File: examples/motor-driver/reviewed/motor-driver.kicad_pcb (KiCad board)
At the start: 2 copper layers, 100 x 50 mm, 12 parts, among them J1 VM 2.7-10.8V, J2 MOTOR A, J3 MOTOR B, J4 LOGIC, U1 DRV8833PW

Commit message: Regenerate the five with stitched pours, silk that speaks, and wires that never double back
All ten variants rebuilt by the fixed generator: reviewed boards carry
ground on both faces with the stitching ring (buck 35 vias, fpga 116),
thru_hole_only front pours, the board id and connector pin names in
silk, and the buck's explicit ground return; the sheets hook power up
through upright symbols and source-anchored flags with no overlapping
wires and no junction-less tees left. Every reviewed variant passes its
own gate with zero errors; every as-generated variant still fails, now
also for the rules this round added.

Co-Authored-By: Claude Fable 5 <noreply@anthropic.com>
Claude-Session: https://claude.ai/code/session_01DUj7Ltu92tWg159mCSacwY
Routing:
- net GND: vias 10 -> 37
- added copper zone on F.Cu, net GND
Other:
- board text added: "AIN1"
- board text added: "AIN2"
- board text added: "AOUT1"
- board text added: "AOUT2"
- board text added: "BIN1"
- board text added: "BIN2"
- board text added: "BOUT1"
- board text added: "BOUT2"
- board text added: "GND"
- board text added: "VM"
- board text added: "VM OK"
- board text added: "motor-driver rev A"
- board text added: "nFAULT"
- board text added: "nSLEEP"
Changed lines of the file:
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@@
 	(via (at 160.75 93.0) (size 0.8) (drill 0.4) (layers "F.Cu" "B.Cu") (net 6))
 	(via (at 163.0 95.25) (size 0.8) (drill 0.4) (layers "F.Cu" "B.Cu") (net 6))
+	(via (at 104.5 64.5) (size 0.8) (drill 0.4) (layers "F.Cu" "B.Cu") (net 1))
+	(via (at 104.5 105.5) (size 0.8) (drill 0.4) (layers "F.Cu" "B.Cu") (net 1))
+	(via (at 114.5 64.5) (size 0.8) (drill 0.4) (layers "F.Cu" "B.Cu") (net 1))
+	(via (at 114.5 105.5) (size 0.8) (drill 0.4) (layers "F.Cu" "B.Cu") (net 1))
+	(via (at 124.5 64.5) (size 0.8) (drill 0.4) (layers "F.Cu" "B.Cu") (net 1))
+	(via (at 124.5 105.5) (size 0.8) (drill 0.4) (layers "F.Cu" "B.Cu") (net 1))
+	(via (at 134.5 64.5) (size 0.8) (drill 0.4) (layers "F.Cu" "B.Cu") (net 1))
+	(via (at 134.5 105.5) (size 0.8) (drill 0.4) (layers "F.Cu" "B.Cu") (net 1))
+	(via (at 144.5 64.5) (size 0.8) (drill 0.4) (layers "F.Cu" "B.Cu") (net 1))
+	(via (at 144.5 105.5) (size 0.8) (drill 0.4) (layers "F.Cu" "B.Cu") (net 1))
+	(via (at 154.5 64.5) (size 0.8) (drill 0.4) (layers "F.Cu" "B.Cu") (net 1))
+	(via (at 154.5 105.5) (size 0.8) (drill 0.4) (layers "F.Cu" "B.Cu") (net 1))
+	(via (at 164.5 64.5) (size 0.8) (drill 0.4) (layers "F.Cu" "B.Cu") (net 1))
+	(via (at 164.5 105.5) (size 0.8) (drill 0.4) (layers "F.Cu" "B.Cu") (net 1))
+	(via (at 174.5 64.5) (size 0.8) (drill 0.4) (layers "F.Cu" "B.Cu") (net 1))
+	(via (at 174.5 105.5) (size 0.8) (drill 0.4) (layers "F.Cu" "B.Cu") (net 1))
+	(via (at 184.5 64.5) (size 0.8) (drill 0.4) (layers "F.Cu" "B.Cu") (net 1))
+	(via (at 184.5 105.5) (size 0.8) (drill 0.4) (layers "F.Cu" "B.Cu") (net 1))
+	(via (at 194.5 64.5) (size 0.8) (drill 0.4) (layers "F.Cu" "B.Cu") (net 1))
+	(via (at 194.5 105.5) (size 0.8) (drill 0.4) (layers "F.Cu" "B.Cu") (net 1))
+	(via (at 104.5 74.5) (size 0.8) (drill 0.4) (layers "F.Cu" "B.Cu") (net 1))
+	(via (at 195.5 74.5) (size 0.8) (drill 0.4) (layers "F.Cu" "B.Cu") (net 1))
+	(via (at 104.5 84.5) (size 0.8) (drill 0.4) (layers "F.Cu" "B.Cu") (net 1))
+	(via (at 195.5 84.5) (size 0.8) (drill 0.4) (layers "F.Cu" "B.Cu") (net 1))
+	(via (at 104.5 94.5) (size 0.8) (drill 0.4) (layers "F.Cu" "B.Cu") (net 1))
+	(via (at 195.5 94.5) (size 0.8) (drill 0.4) (layers "F.Cu" "B.Cu") (net 1))
+	(via (at 195.5 104.5) (size 0.8) (drill 0.4) (layers "F.Cu" "B.Cu") (net 1))
 	(zone
 		(net 1)
@@
 		(polygon (pts (xy 103.0 63.0) (xy 197.0 63.0) (xy 197.0 107.0) (xy 103.0 107.0)))
 	)
+	(zone
+		(net 1)
+		(net_name "GND")
+		(layer "F.Cu")
+		(hatch edge 0.5)
+		(connect_pads thru_hole_only
+			(clearance 0.4)
+		)
+		(min_thickness 0.175)
+		(filled_areas_thickness no)
+		(fill yes
+			(thermal_gap 0.5)
+			(thermal_bridge_width 0.5)
+		)
+		(polygon (pts (xy 103.0 63.0) (xy 197.0 63.0) (xy 197.0 107.0) (xy 103.0 107.0)))
+	)
+	(gr_text "motor-driver rev A" (at 150.0 107.8 0) (layer "F.SilkS") (effects (font (size 1.0 1.0) (thickness 0.15))))
+	(gr_text "VM" (at 185.3 72.0 0) (layer "F.SilkS") (effects (font (size 0.8 0.8) (thickness 0.12))))
+	(gr_text "GND" (at 185.3 77.0 0) (layer "F.SilkS") (effects (font (size 0.8 0.8) (thickness 0.12))))
+	(gr_text "VM OK" (at 180.0 68.6 0) (layer "F.SilkS") (effects (font (size 0.8 0.8) (thickness 0.12))))
+	(gr_text "AOUT2" (at 114.7 80.0 0) (layer "F.SilkS") (effects (font (size 0.8 0.8) (thickness 0.12))))
+	(gr_text "AOUT1" (at 114.7 75.0 0) (layer "F.SilkS") (effects (font (size 0.8 0.8) (thickness 0.12))))
+	(gr_text "BOUT1" (at 114.7 98.0 0) (layer "F.SilkS") (effects (font (size 0.8 0.8) (thickness 0.12))))
+	(gr_text "BOUT2" (at 114.7 93.0 0) (layer "F.SilkS") (effects (font (size 0.8 0.8) (thickness 0.12))))
+	(gr_text "GND" (at 188.63 86.0 0) (layer "F.SilkS") (effects (font (size 0.8 0.8) (thickness 0.12))))
+	(gr_text "nSLEEP" (at 188.63 88.54 0) (layer "F.SilkS") (effects (font (size 0.8 0.8) (thickness 0.12))))
+	(gr_text "AIN1" (at 188.63 91.08 0) (layer "F.SilkS") (effects (font (size 0.8 0.8) (thickness 0.12))))
+	(gr_text "AIN2" (at 188.63 93.62 0) (layer "F.SilkS") (effects (font (size 0.8 0.8) (thickness 0.12))))
+	(gr_text "BIN2" (at 188.63 96.16 0) (layer "F.SilkS") (effects (font (size 0.8 0.8) (thickness 0.12))))
+	(gr_text "BIN1" (at 188.63 98.7 0) (layer "F.SilkS") (effects (font (size 0.8 0.8) (thickness 0.12))))
+	(gr_text "nFAULT" (at 188.63 101.24 0) (layer "F.SilkS") (effects (font (size 0.8 0.8) (thickness 0.12))))
+	(gr_text "GND" (at 188.63 103.78 0) (layer "F.SilkS") (effects (font (size 0.8 0.8) (thickness 0.12))))
 )

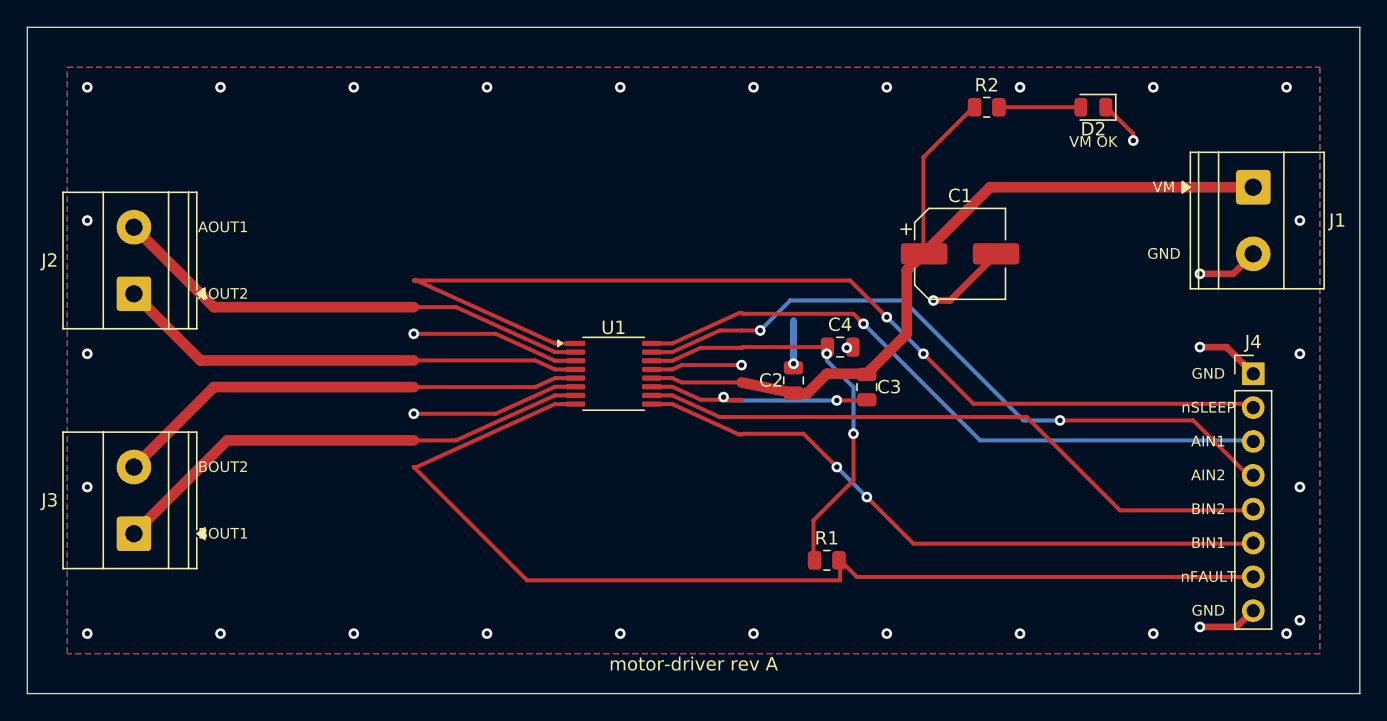
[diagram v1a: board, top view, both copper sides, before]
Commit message: Regenerate the five as round three drew them
All five reviewed projects pass their gates again: the buck all wire
with its feedback drawn home, the motor's logic named at the header,
the carrier reading as the pinout table it is - with its feed diode
finally pointing the right way - the filter compact with test points,
and the FPGA's capacitors sitting beside the units they feed. Thirty
renders redrawn, verdict tables at today's numbers.

Co-Authored-By: Claude Fable 5 <noreply@anthropic.com>
Claude-Session: https://claude.ai/code/session_01DUj7Ltu92tWg159mCSacwY
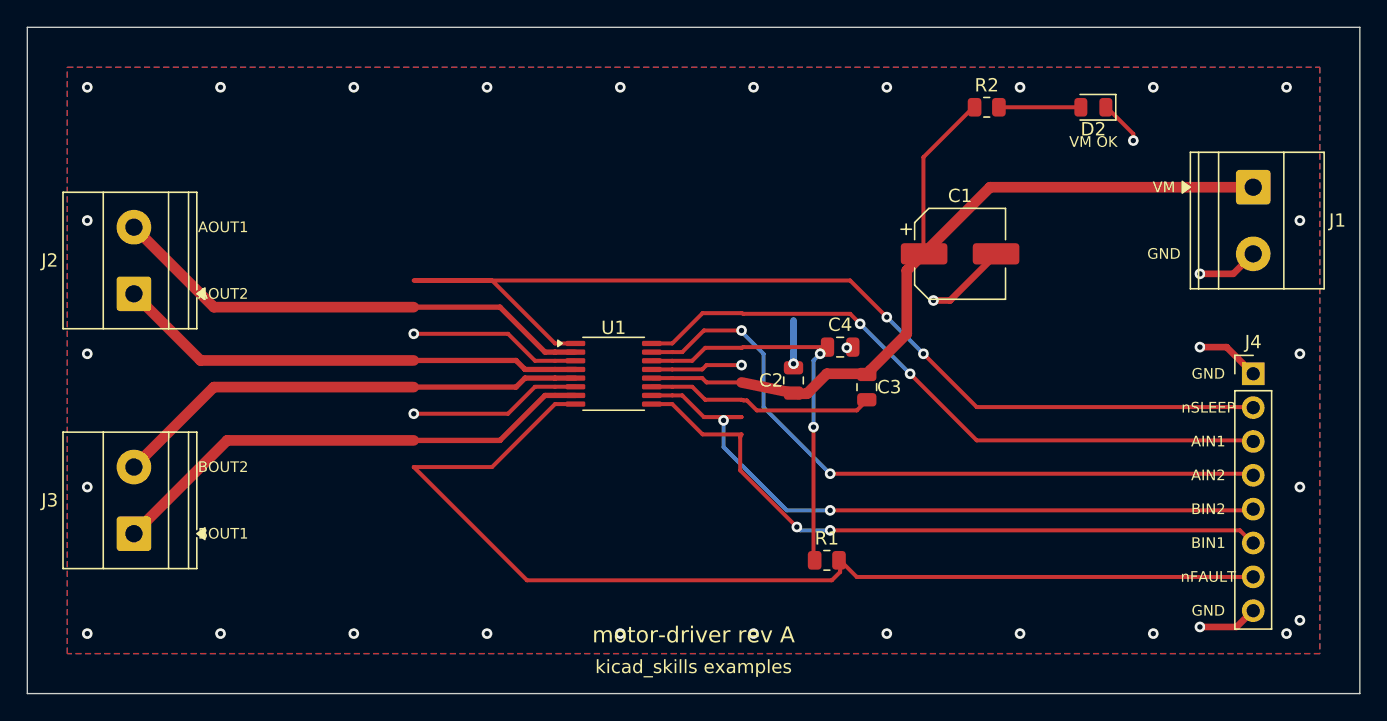
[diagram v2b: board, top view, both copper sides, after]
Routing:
- net /BIN2: track 48.4 -> 52.7 mm, vias 0 -> 2
- net /BIN1: track 49.1 -> 51.1 mm
- net /VCP: track 19.3 -> 17.2 mm, vias 2 -> 0
- net /VINT: track 31.5 -> 30.1 mm
- net /nSLEEP: track 80.1 -> 81.0 mm
- net GND: track 59.5 -> 60.3 mm
- net /AIN2: track 51.8 -> 52.7 mm
- net /BOUT1: track 36.8 -> 37.4 mm
- net /AOUT1: track 36.4 -> 37.0 mm
- net /nFAULT: track 81.8 -> 82.3 mm
- net /AIN1: track 49.6 -> 50.0 mm, vias 1 -> 2
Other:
- board text added: "kicad_skills examples"

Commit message: Regenerate the four boards round four has settled
The buck, the motor driver, the carrier and the filter as the current
generator draws them: interior ground stitching on all four, the motor
driver's bundle tight and its board twelve millimetres shorter, the
filter compact and hand-placed, the carrier's indicator in a column of
its own. All four pass their gates. The FPGA is still regenerating.

Co-Authored-By: Claude Fable 5 <noreply@anthropic.com>
Claude-Session: https://claude.ai/code/session_01DUj7Ltu92tWg159mCSacwY
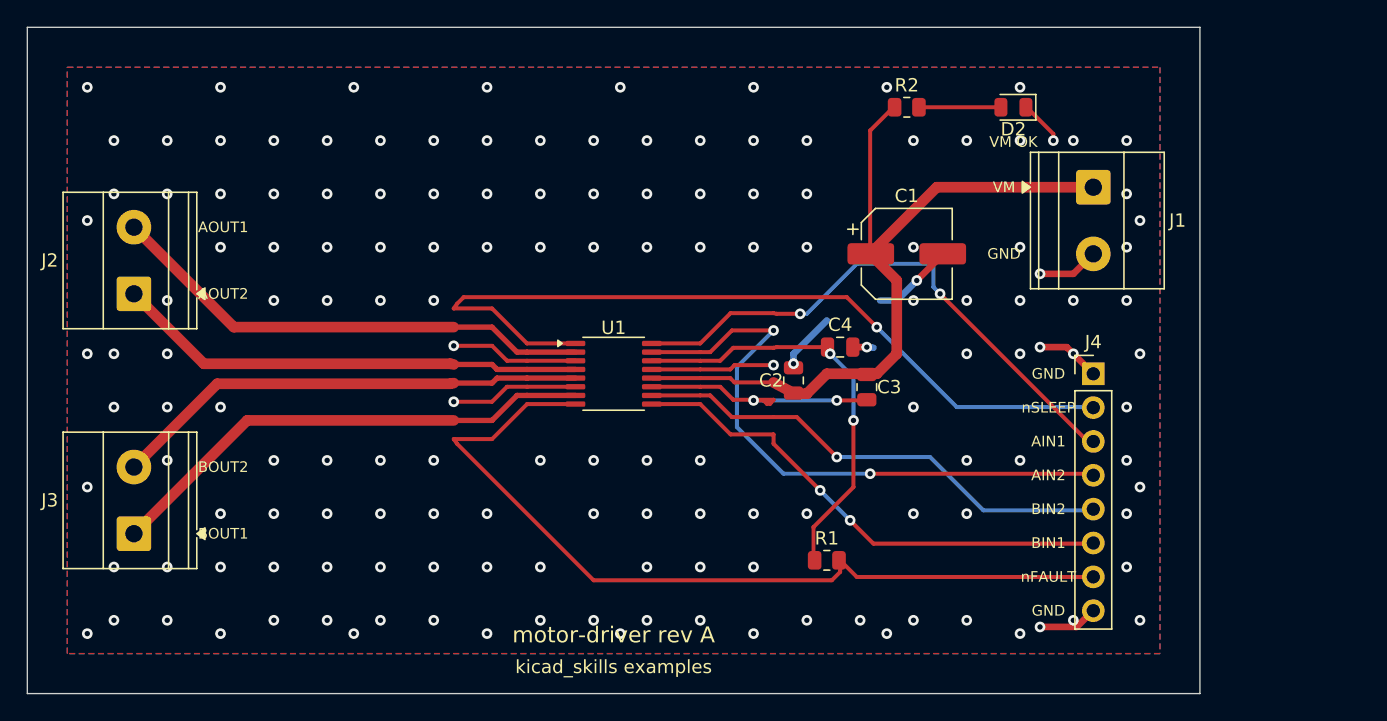
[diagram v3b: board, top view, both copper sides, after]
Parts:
- moved J1 12.0 mm to (180.0, 72.0)
- moved J4 12.0 mm to (180.0, 86.0)
- moved D2 6.00 mm to (174.0, 66.0)
- moved R2 6.00 mm to (166.0, 66.0)
- moved C1 4.00 mm to (166.0, 77.0)
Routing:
- net /nSLEEP: track 81.0 -> 62.0 mm, vias 2 -> 1
- net /nFAULT: track 82.3 -> 64.4 mm
- net /BIN2: track 52.7 -> 36.7 mm, vias 2 -> 1
- net /BIN1: track 51.1 -> 37.9 mm
- net /VM: track 67.2 -> 58.9 mm
- net /AIN1: track 50.0 -> 42.2 mm
- net /AIN2: track 52.7 -> 46.4 mm
- net /VCP: track 17.2 -> 19.8 mm, vias 0 -> 2
- net GND: track 60.3 -> 58.1 mm, vias 37 -> 156
- net /VINT: track 30.1 -> 31.7 mm
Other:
- board size 100 x 50 mm -> 88 x 50 mm

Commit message: Regenerate the four boards whose corners were off the grid
Ninety-one bends at angles nobody chose, now none. All four still pass
their gates.

Co-Authored-By: Claude Fable 5 <noreply@anthropic.com>
Claude-Session: https://claude.ai/code/session_01DUj7Ltu92tWg159mCSacwY
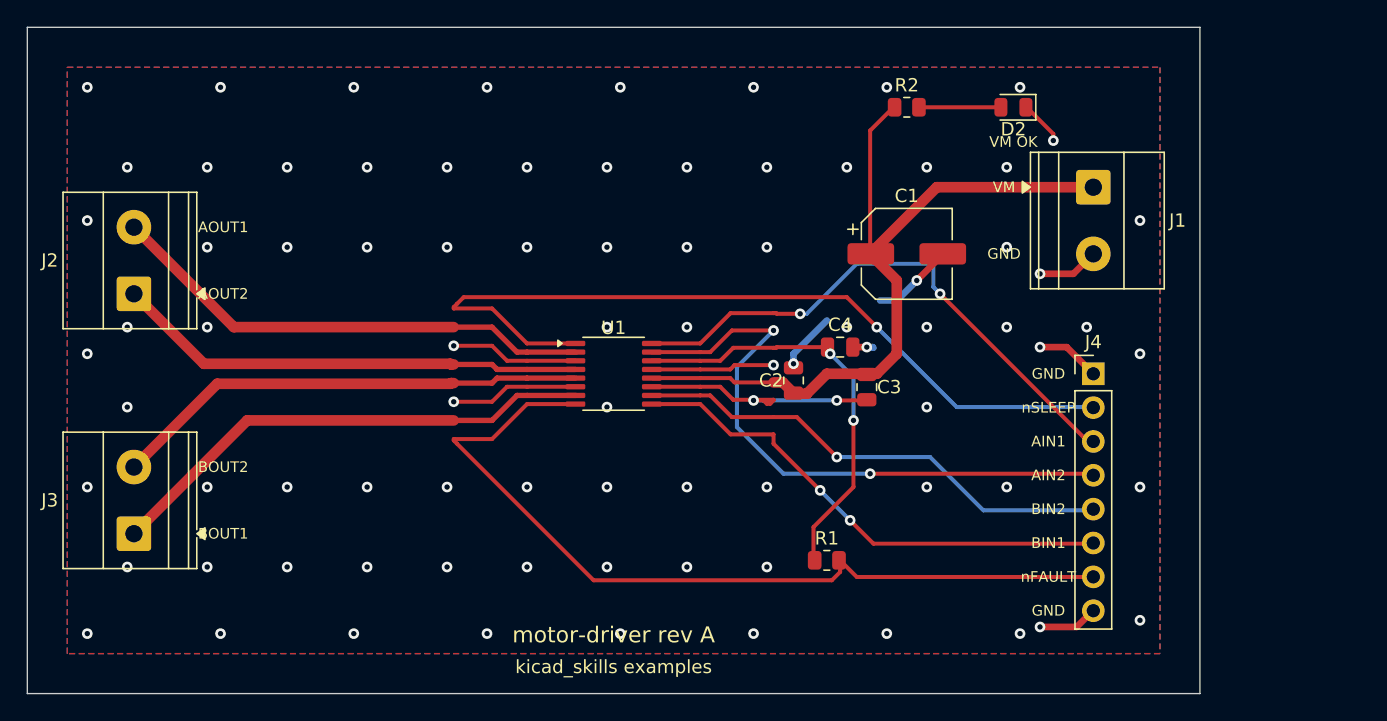
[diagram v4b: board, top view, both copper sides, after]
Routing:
- net GND: track 58.1 -> 58.2 mm, vias 156 -> 84

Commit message: Regenerate the four the text and width work changed
Designators and values off the rails they were printed on, power-named
nets at the width their rule asks for, and the buck's feedback ending
on the capacitor pad it senses at.

Co-Authored-By: Claude Fable 5 <noreply@anthropic.com>
Claude-Session: https://claude.ai/code/session_01DUj7Ltu92tWg159mCSacwY
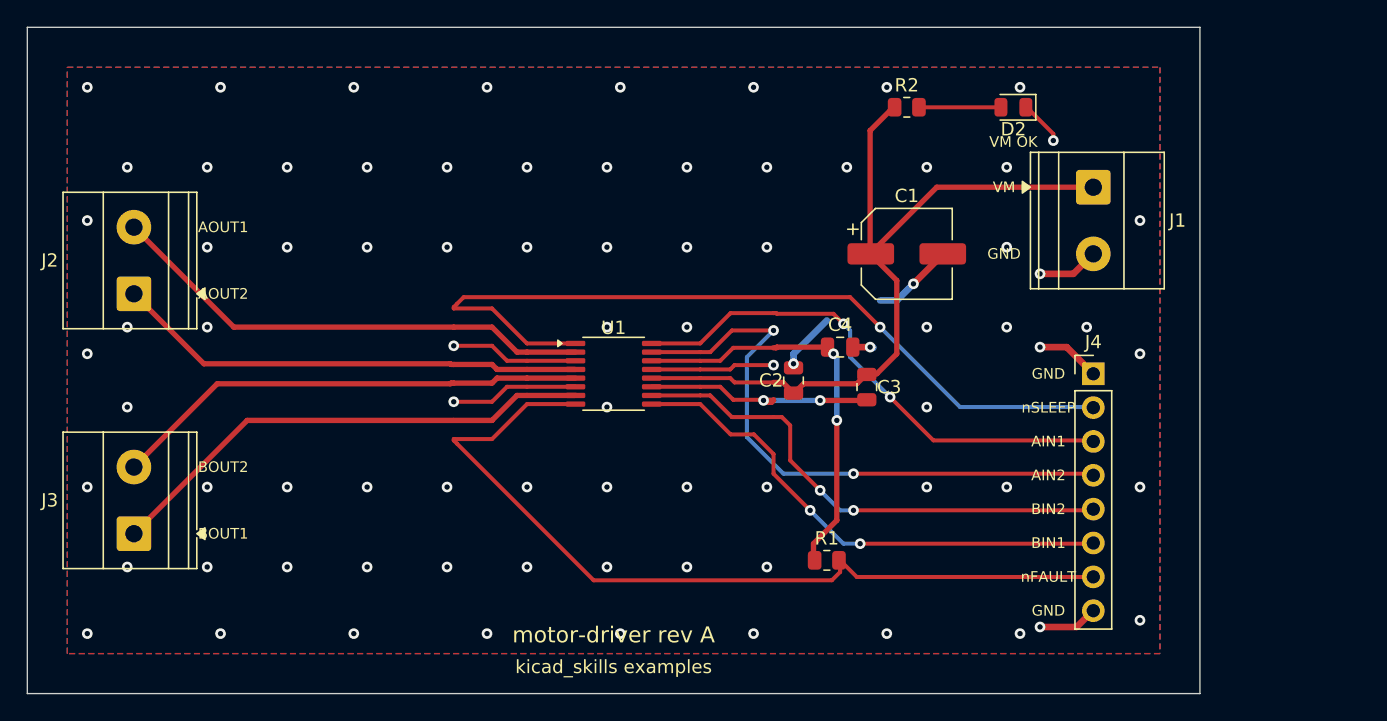
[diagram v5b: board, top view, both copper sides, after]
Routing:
- net /AIN1: track 42.2 -> 39.2 mm
- net /VCP: track 19.8 -> 18.2 mm
- net /BIN2: track 36.7 -> 38.3 mm, vias 1 -> 2
- net /VINT: track 31.7 -> 30.7 mm
- net /AIN2: track 46.4 -> 45.8 mm
- net GND: vias 84 -> 83
